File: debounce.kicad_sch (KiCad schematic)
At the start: 3 parts

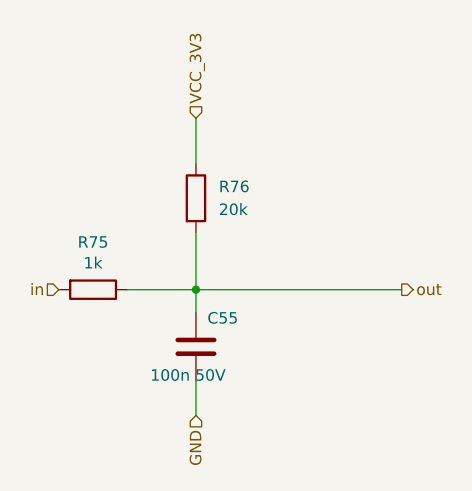
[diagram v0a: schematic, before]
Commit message: Refactored top sheet
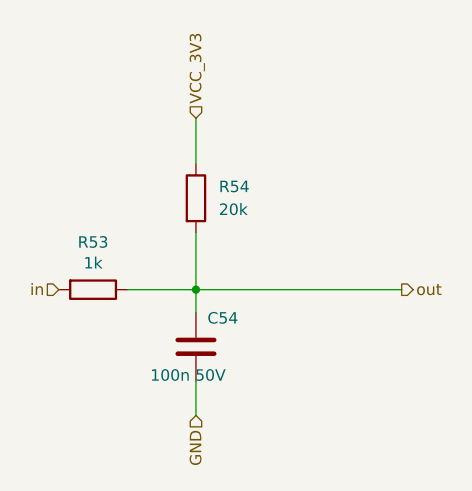
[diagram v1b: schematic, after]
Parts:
- renumbered C55 to C54, R75 to R53, R76 to R54
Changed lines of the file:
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@@
   (symbol (lib_id "Device:R") (at 110.49 86.36 0) (unit 1)
     (in_bom yes) (on_board yes) (fields_autoplaced)
-    (property "Reference" "R76" (id 0) (at 113.03 85.0899 0)
+    (property "Reference" "R54" (id 0) (at 113.03 85.0899 0)
       (effects (font (size 1.27 1.27)) (justify left))
     )
@@
   (symbol (lib_id "Device:R") (at 99.06 96.52 270) (unit 1)
     (in_bom yes) (on_board yes)
-    (property "Reference" "R75" (id 0) (at 99.06 91.2622 90))
+    (property "Reference" "R53" (id 0) (at 99.06 91.2622 90))
     (property "Value" "1k" (id 1) (at 99.06 93.5736 90))
     (property "Footprint" "Resistor_SMD:R_1206_3216Metric" (id 2) (at 99.06 94.742 90)
@@
   (symbol (lib_id "Device:C") (at 110.49 102.87 0) (unit 1)
     (in_bom yes) (on_board yes)
-    (property "Reference" "C55" (id 0) (at 111.76 99.6949 0)
+    (property "Reference" "C54" (id 0) (at 111.76 99.6949 0)
       (effects (font (size 1.27 1.27)) (justify left))
     )
